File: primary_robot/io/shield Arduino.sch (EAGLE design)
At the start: 40 parts

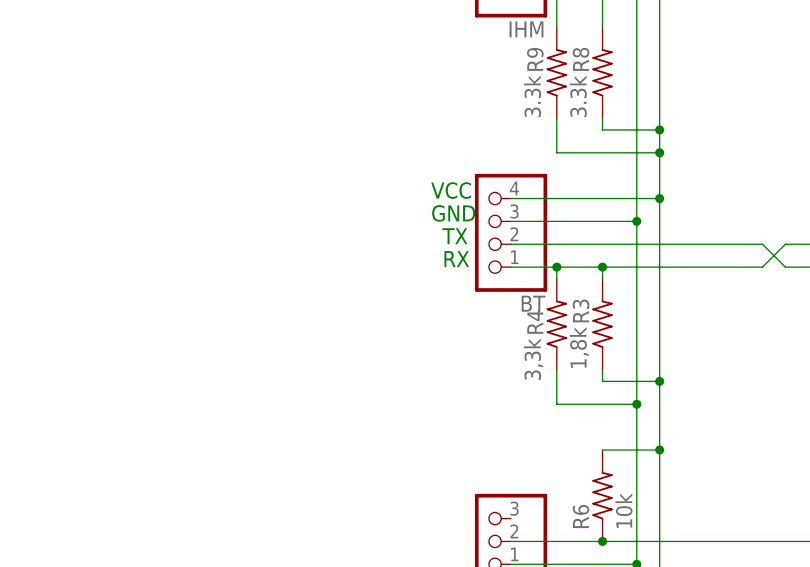
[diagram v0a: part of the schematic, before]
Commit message: [priom/io] Updates some labels
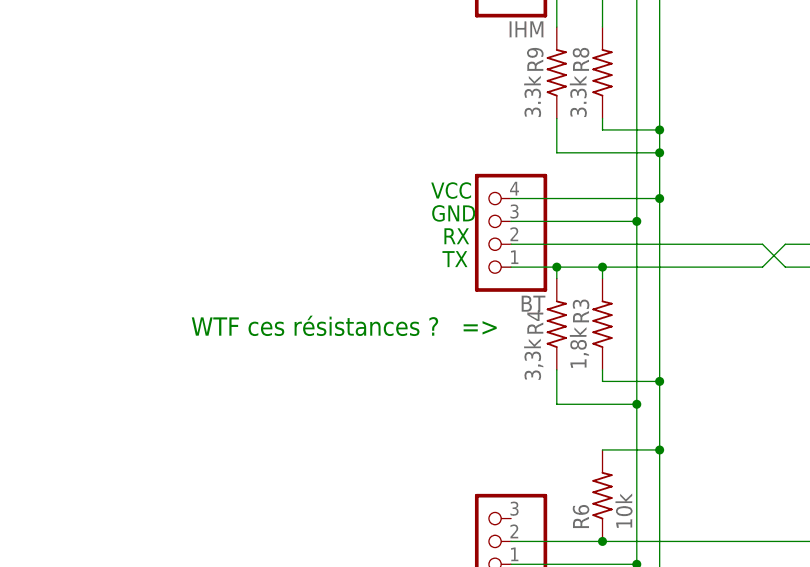
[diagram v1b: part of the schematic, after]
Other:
- note added: "WTF ces résistances ? =>"
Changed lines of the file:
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@@
 <text x="200.66" y="-3.81" size="1.778" layer="91">0 RX</text>
 <text x="200.66" y="-1.27" size="1.778" layer="91">1 TX</text>
-<text x="50.8" y="-40.64" size="1.778" layer="91">RX</text>
-<text x="50.8" y="-38.1" size="1.778" layer="91">TX</text>
+<text x="50.8" y="-40.64" size="1.778" layer="91">TX</text>
+<text x="50.8" y="-38.1" size="1.778" layer="91">RX</text>
 <text x="200.66" y="1.27" size="1.778" layer="91">2</text>
 <text x="200.66" y="3.81" size="1.778" layer="91">3</text>
@@
 <text x="10.16" y="-114.3" size="1.778" layer="91">SCL</text>
 <text x="213.36" y="22.86" size="5.08" layer="91">!! Utiliser une lib arduino pour éviter les problèmes !!</text>
+<text x="22.86" y="-48.26" size="2.032" layer="91">WTF ces résistances ?   =&gt;</text>
 </plain>
 <instances>
